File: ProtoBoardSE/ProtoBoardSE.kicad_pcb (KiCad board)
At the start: 2 copper layers, 48 x 56 mm, 32 parts, among them J1 TYPE-C-31-M-12, J10 Conn_01x05, J11 Conn_01x05_Female, J2 TYPE-C-31-M-12, J3 Conn_01x10_Female, J4 Conn_01x05_Female, J5 Conn_01x05, J6 Conn_01x05, J7 Conn_01x05_Female, J8 Conn_01x05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

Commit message: ProtoBoard SE : fix servo connector alignement
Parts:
- moved J11 0.92 mm to (188.1, 79.9)
- moved J7 0.46 mm to (188.1, 82.5)
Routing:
- net /VBUS0: track 41.0 -> 40.0 mm
- net /Servo5: track 31.7 -> 32.7 mm
- net /Servo4: track 29.9 -> 30.8 mm
- net /Servo3: track 28.1 -> 29.0 mm
- net /Servo2: track 26.2 -> 27.1 mm
- net /VBUS1: track 30.0 -> 29.1 mm
- net /CH12: track 26.6 -> 25.7 mm
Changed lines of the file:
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@@
   )
   (footprint "Connector_PinHeader_2.54mm:PinHeader_1x05_P2.54mm_Vertical" (layer "F.Cu")
-    (at 188.075 82 -90)
+    (at 188.075 82.46 -90)
     (descr "Through hole straight pin header, 1x05, 2.54mm pitch, single row")
     (tags "Through hole pin header THT 1x05 2.54mm single row")
@@
   )
   (footprint "Connector_PinHeader_2.54mm:PinHeader_1x05_P2.54mm_Vertical" (layer "F.Cu")
-    (at 188.075 79 -90)
+    (at 188.075 79.92 -90)
     (descr "Through hole straight pin header, 1x05, 2.54mm pitch, single row")
     (tags "Through hole pin header THT 1x05 2.54mm single row")
@@
     (property "Sheetname" "")
     (attr exclude_from_pos_files)
-    (fp_text reference "H4" (at 0 -3.2) (layer "F.SilkS")
+    (fp_text reference "H4" (at 0 -3.2) (layer "F.SilkS") hide
       (effects (font (size 1 1) (thickness 0.15)))
     )
@@
   )
   (dimension (type aligned) (layer "Margin")
+    (pts (xy 188.075 85) (xy 188.075 82.46))
+    (height -0.242)
+    (gr_text "2.5400 mm" (at 186.683 83.73 90) (layer "Margin")
+      (effects (font (size 1 1) (thickness 0.15)))
+    )
+    (format (units 3) (units_format 1) (precision 4))
+    (style (thickness 0.15) (arrow_length 1.27) (text_position_mode 0) (extension_height 0.58642) (extension_offset 0.5) keep_text_aligned)
+  )
+  (dimension (type aligned) (layer "Margin")
     (pts (xy 160 30) (xy 160 86))
     (height 22.125)
@@
     (height -12)
     (gr_text "48.0000 mm" (at 184 16.85) (layer "Margin")
+      (effects (font (size 1 1) (thickness 0.15)))
+    )
+    (format (units 3) (units_format 1) (precision 4))
+    (style (thickness 0.15) (arrow_length 1.27) (text_position_mode 0) (extension_height 0.58642) (extension_offset 0.5) keep_text_aligned)
+  )
+  (dimension (type aligned) (layer "Margin")
+    (pts (xy 188.075 79.92) (xy 188.075 82.46))
+    (height -2.679)
+    (gr_text "2.5400 mm" (at 189.604 81.19 90) (layer "Margin")
       (effects (font (size 1 1) (thickness 0.15)))
     )
@@
   (segment (start 190.25 46.5) (end 190.25 48.25) (width 1) (layer "B.Cu") (net 3))
   (segment (start 191.25 80.5) (end 189.75 82) (width 0.5) (layer "F.Cu") (net 4))
-  (segment (start 188.075 82) (end 177.915 82) (width 1) (layer "F.Cu") (net 4))
   (segment (start 199.256522 76.25) (end 193 76.25) (width 0.5) (layer "F.Cu") (net 4))
+  (segment (start 189.828 82.46) (end 191.008 81.28) (width 1) (layer "F.Cu") (net 4))
   (segment (start 190.75 82) (end 192 80.75) (width 0.5) (layer "F.Cu") (net 4))
   (segment (start 200.7 77.693478) (end 199.256522 76.25) (width 0.5) (layer "F.Cu") (net 4))
+  (segment (start 188.075 82.46) (end 189.828 82.46) (width 1) (layer "F.Cu") (net 4))
   (segment (start 200.7 78.7675) (end 200.7 77.693478) (width 0.5) (layer "F.Cu") (net 4))
-  (segment (start 188.075 82) (end 190.75 82) (width 0.5) (layer "F.Cu") (net 4))
   (segment (start 192 78.25) (end 193.25 77) (width 0.5) (layer "F.Cu") (net 4))
+  (segment (start 177.915 82.46) (end 188.075 82.46) (width 1) (layer "F.Cu") (net 4))
   (segment (start 195.156522 77) (end 195.8 77.643478) (width 0.5) (layer "F.Cu") (net 4))
   (segment (start 193 76.25) (end 191.25 78) (width 0.5) (layer "F.Cu") (net 4))
   (segment (start 193.25 77) (end 195.156522 77) (width 0.5) (layer "F.Cu") (net 4))
-  (segment (start 189.75 82) (end 188.075 82) (width 1) (layer "F.Cu") (net 4))
   (segment (start 192 80.75) (end 192 78.25) (width 0.5) (layer "F.Cu") (net 4))
   (segment (start 191.25 78) (end 191.25 80.5) (width 0.5) (layer "F.Cu") (net 4))
@@
   (segment (start 200.7 38.45) (end 200.75 38.5) (width 0.5) (layer "F.Cu") (net 11))
   (segment (start 195.8 38.45) (end 195.75 38.5) (width 0.5) (layer "F.Cu") (net 11))
-  (segment (start 179.3 43.5) (end 179.1 43.3) (width 0.5) (layer "F.Cu") (net 11))
   (segment (start 179.02 43.38) (end 179.1 43.3) (width 0.25) (layer "F.Cu") (net 11))
   (segment (start 192 43.5) (end 179.3 43.5) (width 0.5) (layer "F.Cu") (net 11))
   (segment (start 195.8 37.2325) (end 195.8 38.45) (width 0.5) (layer "F.Cu") (net 11))
   (segment (start 179.02 45.5) (end 179.02 43.38) (width 0.25) (layer "F.Cu") (net 11))
-  (segment (start 179.55 43.75) (end 179.1 43.3) (width 0.5) (layer "F.Cu") (net 11))
   (via (at 200.75 38.5) (size 0.8) (drill 0.4) (layers "F.Cu" "B.Cu") (net 11))
   (via (at 195.75 38.5) (size 0.8) (drill 0.4) (layers "F.Cu" "B.Cu") (net 11))
@@
   (segment (start 195.5 63.75) (end 193.75 62) (width 0.25) (layer "B.Cu") (net 35))
   (segment (start 195.5 75.5) (end 195.5 63.75) (width 0.25) (layer "B.Cu") (net 35))
-  (segment (start 188.075 79) (end 192 79) (width 0.25) (layer "B.Cu") (net 35))
+  (segment (start 188.075 79.92) (end 188.075 79.895) (width 0.25) (layer "B.Cu") (net 35))
+  (segment (start 188.97 79) (end 192 79) (width 0.25) (layer "B.Cu") (net 35))
   (segment (start 192 79) (end 195.5 75.5) (width 0.25) (layer "B.Cu") (net 35))
+  (segment (start 188.075 79.895) (end 188.97 79) (width 0.25) (layer "B.Cu") (net 35))
   (segment (start 192.5 62) (end 192.5 63.36) (width 0.25) (layer "F.Cu") (net 36))
   (segment (start 192.5 63.36) (end 192.64 63.5) (width 0.25) (layer "F.Cu") (net 36))
@@
   (segment (start 194.75 74.75) (end 194.75 64.75) (width 0.25) (layer "B.Cu") (net 36))
   (segment (start 185.535 79) (end 186.785 77.75) (width 0.25) (layer "B.Cu") (net 36))
+  (segment (start 185.535 79) (end 185.535 79.92) (width 0.25) (layer "B.Cu") (net 36))
   (segment (start 191.75 77.75) (end 194.75 74.75) (width 0.25) (layer "B.Cu") (net 36))
   (segment (start 191.25 63.38) (end 191.37 63.5) (width 0.25) (layer "F.Cu") (net 37))
   (segment (start 191.25 62) (end 191.25 63.38) (width 0.25) (layer "F.Cu") (net 37))
   (via (at 191.25 62) (size 0.8) (drill 0.4) (layers "F.Cu" "B.Cu") (net 37))
+  (segment (start 182.995 79) (end 182.995 79.92) (width 0.25) (layer "B.Cu") (net 37))
   (segment (start 184.995 77) (end 191.5 77) (width 0.25) (layer "B.Cu") (net 37))
   (segment (start 194 74.5) (end 194 64.75) (width 0.25) (layer "B.Cu") (net 37))
@@
   (segment (start 183.205 76.25) (end 191.25 76.25) (width 0.25) (layer "B.Cu") (net 38))
   (segment (start 193.25 74.25) (end 193.25 65.25) (width 0.25) (layer "B.Cu") (net 38))
+  (segment (start 180.455 79) (end 180.455 79.92) (width 0.25) (layer "B.Cu") (net 38))
   (segment (start 191.25 76.25) (end 193.25 74.25) (width 0.25) (layer "B.Cu") (net 38))
   (segment (start 193.25 65.25) (end 190 62) (width 0.25) (layer "B.Cu") (net 38))
@@
   (segment (start 191 75.5) (end 192.5 74) (width 0.25) (layer "B.Cu") (net 39))
   (segment (start 177.915 79) (end 181.415 75.5) (width 0.25) (layer "B.Cu") (net 39))
+  (segment (start 177.915 79) (end 177.915 79.92) (width 0.25) (layer "B.Cu") (net 39))
   (segment (start 192.5 74) (end 192.5 65.75) (width 0.25) (layer "B.Cu") (net 39))
   (segment (start 195.18 63.5) (end 195.18 62.07) (width 0.25) (layer "F.Cu") (net 40))
@@
   (segment (start 190.25 72.344592) (end 189.452704 71.547296) (width 0.25) (layer "B.Cu") (net 56))
   (segment (start 179 70.75) (end 180.25 69.5) (width 0.25) (layer "B.Cu") (net 56))
-  (segment (start 189.405408 71.5) (end 189.874011 71.968603) (width 0.25) (layer "B.Cu") (net 56))
   (segment (start 189 71.5) (end 189.405408 71.5) (width 0.25) (layer "B.Cu") (net 56))
   (segment (start 185.5 71.5) (end 189 71.5) (width 0.25) (layer "B.Cu") (net 56))
-  (segment (start 190.25 72.5) (end 190.25 72.344592) (width 0.25) (layer "B.Cu") (net 56))
   (segment (start 190.375 73.399614) (end 191.25 72.524614) (width 0.25) (layer "F.Cu") (net 57))
   (segment (start 191.25 72.524614) (end 191.25 72.25) (width 0.25) (layer "F.Cu") (net 57))

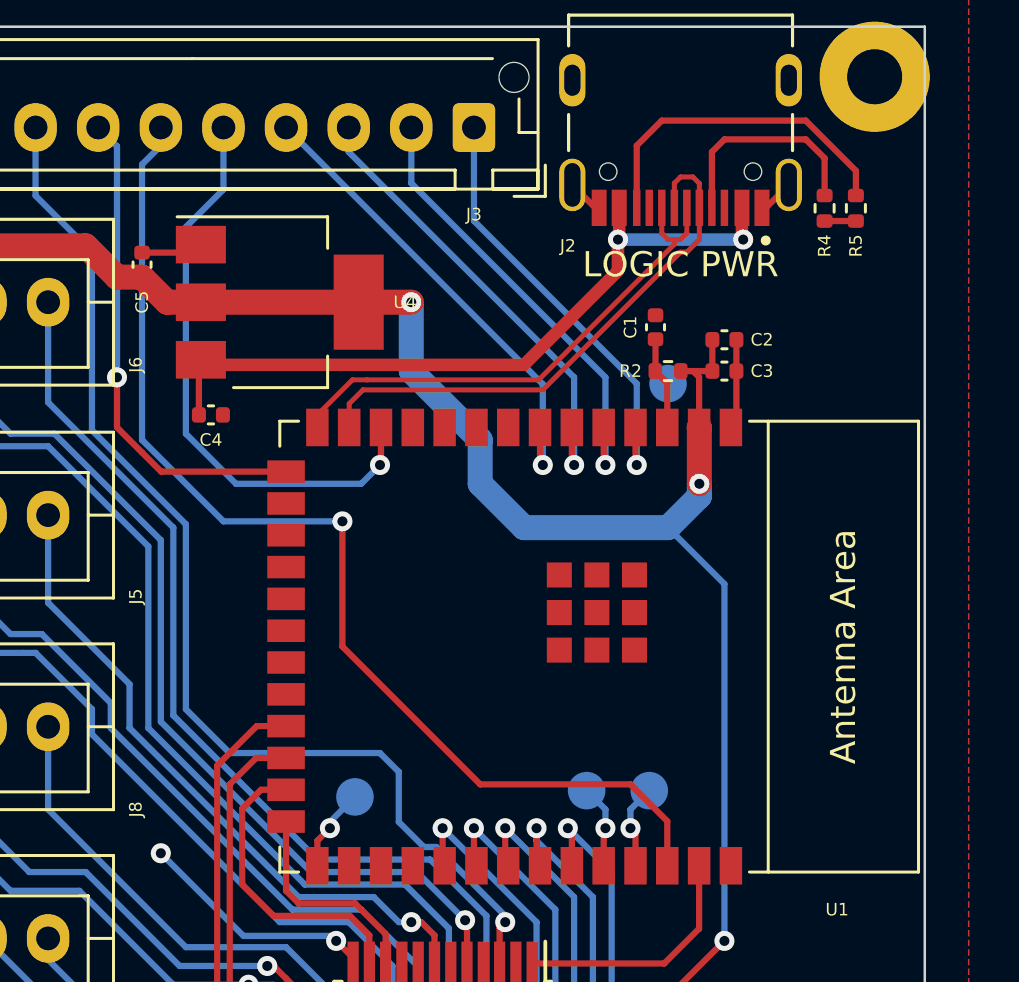
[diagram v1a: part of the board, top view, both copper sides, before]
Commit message: ProtoBoard SE : fix capacitor value and add reset/boot button
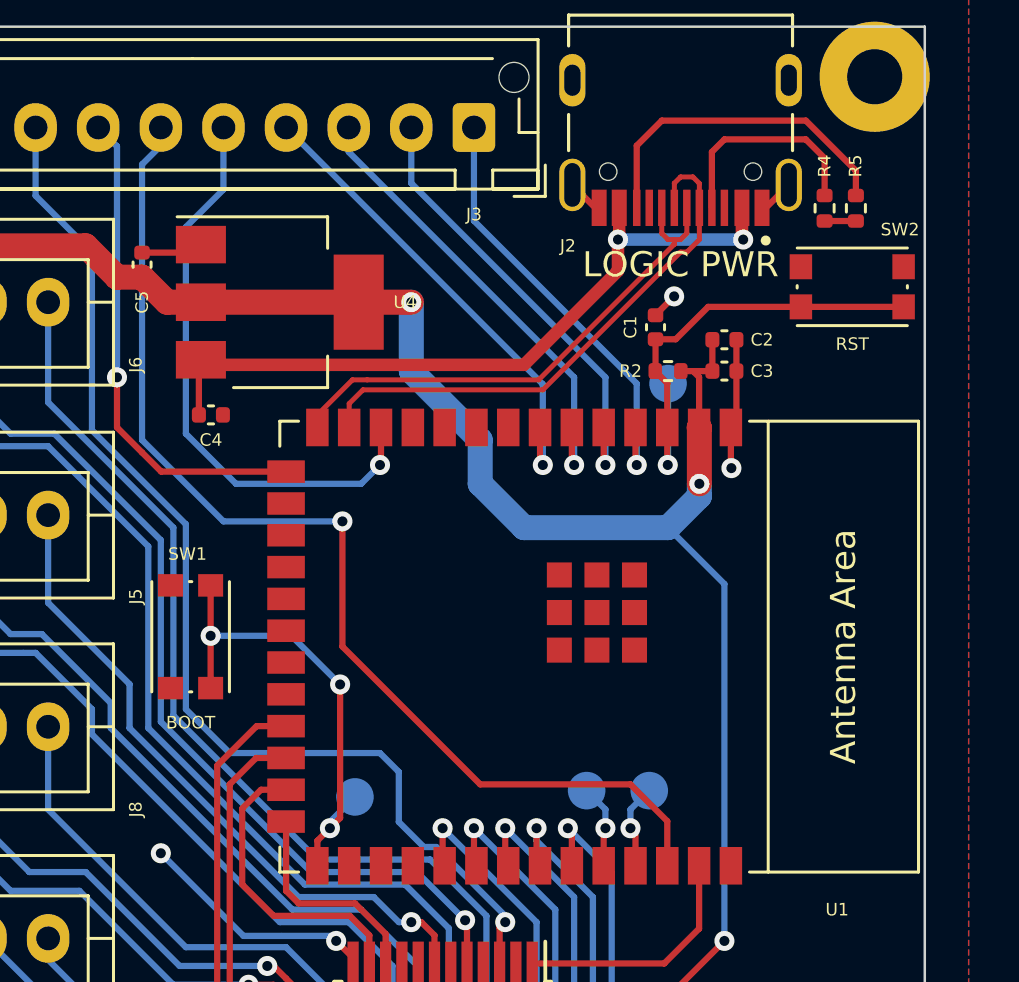
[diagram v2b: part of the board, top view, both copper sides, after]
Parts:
- added SW1: SW_Push, Button_Switch_SMD:SW_Push_1P1T_NO_CK_KMR2, F.Cu at (178.7, 54.4)
- added SW2: SW_Push, Button_Switch_SMD:SW_Push_1P1T_NO_CK_KMR2, F.Cu at (205.1, 40.4)
- C5: value 22uF -> 10uF
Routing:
- net /BOOT0: track 3.37 -> 19.4 mm, vias 1 -> 3
- net /EN: track 3.72 -> 18.9 mm, vias 0 -> 1
- net GND: track 48.7 -> 51.4 mm, vias 3 -> 5
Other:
- board text added: "BOOT"
- board text added: "RST"

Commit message: ProtoBoard SE : part sourcing
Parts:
- added C6: 0.1uF, Capacitor_SMD:C_0402_1005Metric, F.Cu at (194.9, 74.5)
- J10, J5, J6, J8, J9: footprint Connector_JST:JST_XA_B05B-XASK-1-A_1x05_P2.50mm_Vertical -> Connector_JST:JST_XH_B5B-XH-AM_1x05_P2.50mm_Vertical
- U1: value ESP32-S3-WROOM-2 -> ESP32-S3-WROOM-1; footprint Espressif:ESP32-S3-WROOM-2 -> Espressif:ESP32-S3-WROOM-1
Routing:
- net +3V3: track 120.4 -> 122.0 mm

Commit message: ProtoBoard SE : production files for JLCPCB
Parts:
- H1, H2, H3, H4: footprint MountingHole:MountingHole_2.2mm_M2_Pad -> MountingHole:MountingHole_2.2mm_M2
